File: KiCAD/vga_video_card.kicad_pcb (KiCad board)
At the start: 4 copper layers, 87 parts, among them J1 DE15_Socket_HighDensity, J2 Conn_01x20, J3 Conn_01x20, J4 Conn_01x20, J5 Conn_01x20, J6 Conn_02x20_Odd_Even, SW1 rst_btn, SW2 SW_DPDT_x2, SW3 SW_DPDT_x2, SW4 SW_DPDT_x2, U1 74HC161, U10 74HC04, U11 74HC112, U12 74HC32, U13 74HC173, U14 74HC173, U15 74HC161, U16 74HC161, U17 74HC161, U18 74HC04, U19 74HC04, U2 74HC161, U20 74HC133, U21 74HC133, U22 74HC133, U23 74HC133, U24 74HC112, U25 74HC173, U26 74HC173, U27 74HC04, U28 74HC253, U29 74HC253, U3 74HC161, U30 CY7C199, U31 CY7C199, U32 74AHC595, U33 74AHC595, U34 74AHC595, U35 AD7523JN, U36 LM358, U37 74HC257, U38 74HC257, U39 74HC02, U4 74HC04, U40 74HC74, U41 74HC00, U44 74HC257, U45 74HC257, U46 74HC257, U47 74HC257, U48 74HC257, U49 74HC257, U5 74HC04, U50 74HC257, U51 74HC257, U52 74HC4053, U53 74HC4053, U54 74HC4053, U55 74HC257, U56 74HC257, U6 74HC30, U7 74HC30, U8 74HC30, U9 74HC30, Y1 10MHz

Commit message: partially finished pcb layout
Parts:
- moved U28 278.1 mm to (74.9, 49.5), turned to 90 degrees
- moved U29 265.6 mm to (99.1, 49.5), turned to 90 degrees
- moved J5 255.2 mm to (77.5, 193.0), turned to 90 degrees
- moved U32 248.5 mm to (77.5, 165.1)
- moved J3 244.1 mm to (77.5, 186.7), turned to 90 degrees
- moved U40 243.7 mm to (132.1, 154.9)
- moved U33 240.9 mm to (97.8, 165.1)
- moved R4 237.4 mm to (88.9, 182.9), turned to 90 degrees
- moved R2 236.1 mm to (88.9, 172.7), turned to 90 degrees
- moved U34 233.5 mm to (118.1, 165.1)
- moved U41 231.9 mm to (132.1, 111.8)
- moved R5 230.9 mm to (94.0, 182.9), turned to 90 degrees
- moved RV1 230.4 mm to (127.0, 80.0)
- moved R3 229.6 mm to (94.0, 172.7), turned to 90 degrees
- moved J4 226.9 mm to (77.5, 154.9), turned to 90 degrees
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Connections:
- net /RAM_module/RAM_bus_mux/j_addr0 renamed /RAM_module/r_j_addr0
- J6 pad 10: /RAM_module/RAM_bus_mux/j_addr3 -> /RAM_module/r_j_addr3
- J6 pad 11: /RAM_module/RAM_bus_mux/i_addr4 -> /RAM_module/r_i_addr4
- J6 pad 12: /RAM_module/RAM_bus_mux/j_addr4 -> /RAM_module/r_j_addr4
- J6 pad 13: /RAM_module/RAM_bus_mux/i_addr5 -> /RAM_module/r_i_addr5
- J6 pad 14: /RAM_module/RAM_bus_mux/j_addr5 -> /RAM_module/r_j_addr5
- J6 pad 15: /RAM_module/RAM_bus_mux/i_addr6 -> /RAM_module/r_i_addr6
- J6 pad 16: /RAM_module/RAM_bus_mux/j_addr6 -> /RAM_module/r_j_addr6
- J6 pad 17: /RAM_module/RAM_bus_mux/i_addr7 -> /RAM_module/r_i_addr7
- J6 pad 18: /RAM_module/RAM_bus_mux/j_addr7 -> /RAM_module/r_j_addr7
- J6 pad 3: /RAM_module/RAM_bus_mux/i_addr0 -> /RAM_module/r_i_addr0
- J6 pad 5: /RAM_module/RAM_bus_mux/i_addr1 -> /RAM_module/r_i_addr1
- J6 pad 6: /RAM_module/RAM_bus_mux/j_addr1 -> /RAM_module/r_j_addr1
- J6 pad 7: /RAM_module/RAM_bus_mux/i_addr2 -> /RAM_module/r_i_addr2
- J6 pad 8: /RAM_module/RAM_bus_mux/j_addr2 -> /RAM_module/r_j_addr2
- J6 pad 9: /RAM_module/RAM_bus_mux/i_addr3 -> /RAM_module/r_i_addr3
- U13 pad 4: /RAM_module/RAM_bus_mux/j_addr1 -> /RAM_module/r_j_addr1
- U13 pad 5: /RAM_module/RAM_bus_mux/j_addr2 -> /RAM_module/r_j_addr2
- U13 pad 6: /RAM_module/RAM_bus_mux/j_addr3 -> /RAM_module/r_j_addr3
- U14 pad 3: /RAM_module/RAM_bus_mux/j_addr4 -> /RAM_module/r_j_addr4
- U14 pad 4: /RAM_module/RAM_bus_mux/j_addr5 -> /RAM_module/r_j_addr5
- U14 pad 5: /RAM_module/RAM_bus_mux/j_addr6 -> /RAM_module/r_j_addr6
- U14 pad 6: /RAM_module/RAM_bus_mux/j_addr7 -> /RAM_module/r_j_addr7
- U25 pad 3: /RAM_module/RAM_bus_mux/i_addr0 -> /RAM_module/r_i_addr0
- U25 pad 4: /RAM_module/RAM_bus_mux/i_addr1 -> /RAM_module/r_i_addr1
- U25 pad 5: /RAM_module/RAM_bus_mux/i_addr2 -> /RAM_module/r_i_addr2
- U25 pad 6: /RAM_module/RAM_bus_mux/i_addr3 -> /RAM_module/r_i_addr3
- U26 pad 3: /RAM_module/RAM_bus_mux/i_addr4 -> /RAM_module/r_i_addr4
- U26 pad 4: /RAM_module/RAM_bus_mux/i_addr5 -> /RAM_module/r_i_addr5
- U26 pad 5: /RAM_module/RAM_bus_mux/i_addr6 -> /RAM_module/r_i_addr6
- U26 pad 6: /RAM_module/RAM_bus_mux/i_addr7 -> /RAM_module/r_i_addr7
- U44 pad 11: /RAM_module/RAM_bus_mux/addr3 -> /RAM_module/r_i_addr3
- U44 pad 14: /RAM_module/RAM_bus_mux/addr2 -> /RAM_module/r_i_addr2
- U44 pad 2: /RAM_module/RAM_bus_mux/addr0 -> /RAM_module/r_i_addr0
- U44 pad 5: /RAM_module/RAM_bus_mux/addr1 -> /RAM_module/r_i_addr1
- U45 pad 11: /RAM_module/RAM_bus_mux/addr7 -> /RAM_module/r_i_addr7
- U45 pad 14: /RAM_module/RAM_bus_mux/addr6 -> /RAM_module/r_i_addr6
- U45 pad 2: /RAM_module/RAM_bus_mux/addr4 -> /RAM_module/r_i_addr4
- U45 pad 5: /RAM_module/RAM_bus_mux/addr5 -> /RAM_module/r_i_addr5
- U46 pad 11: /RAM_module/RAM_bus_mux/addr11 -> /RAM_module/r_j_addr4
- U46 pad 14: /RAM_module/RAM_bus_mux/addr10 -> /RAM_module/r_j_addr3
- U46 pad 2: /RAM_module/RAM_bus_mux/addr8 -> /RAM_module/r_j_addr1
- U46 pad 5: /RAM_module/RAM_bus_mux/addr9 -> /RAM_module/r_j_addr2
- U47 pad 14: /RAM_module/RAM_bus_mux/addr14 -> /RAM_module/r_j_addr7
- U47 pad 2: /RAM_module/RAM_bus_mux/addr12 -> /RAM_module/r_j_addr5
- U47 pad 5: /RAM_module/RAM_bus_mux/addr13 -> /RAM_module/r_j_addr6
- U48 pad 10: /RAM_module/RAM_bus_mux/addr3 -> /RAM_module/r_i_addr3
- U48 pad 13: /RAM_module/RAM_bus_mux/addr2 -> /RAM_module/r_i_addr2
- U48 pad 3: /RAM_module/RAM_bus_mux/addr0 -> /RAM_module/r_i_addr0
- U48 pad 6: /RAM_module/RAM_bus_mux/addr1 -> /RAM_module/r_i_addr1
- U49 pad 10: /RAM_module/RAM_bus_mux/addr7 -> /RAM_module/r_i_addr7
- U49 pad 13: /RAM_module/RAM_bus_mux/addr6 -> /RAM_module/r_i_addr6
- U49 pad 3: /RAM_module/RAM_bus_mux/addr4 -> /RAM_module/r_i_addr4
- U49 pad 6: /RAM_module/RAM_bus_mux/addr5 -> /RAM_module/r_i_addr5
- U50 pad 10: /RAM_module/RAM_bus_mux/addr11 -> /RAM_module/r_j_addr4
- U50 pad 13: /RAM_module/RAM_bus_mux/addr10 -> /RAM_module/r_j_addr3
- U50 pad 3: /RAM_module/RAM_bus_mux/addr8 -> /RAM_module/r_j_addr1
- U50 pad 6: /RAM_module/RAM_bus_mux/addr9 -> /RAM_module/r_j_addr2
- U51 pad 13: /RAM_module/RAM_bus_mux/addr14 -> /RAM_module/r_j_addr7
- U51 pad 3: /RAM_module/RAM_bus_mux/addr12 -> /RAM_module/r_j_addr5
- U51 pad 6: /RAM_module/RAM_bus_mux/addr13 -> /RAM_module/r_j_addr6
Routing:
- net +5V: track 0.00 -> 1217.3 mm, vias 0 -> 2
- net GND: track 0.00 -> 1176.5 mm
- net /RAM_module/r_j_addr0: track 0.00 -> 338.4 mm, vias 0 -> 4
- net /RAM_module/r_j_addr3: track 0.00 -> 281.1 mm, vias 0 -> 4
- net /RAM_module/r_j_addr7: track 0.00 -> 276.0 mm, vias 0 -> 2
- net /RAM_module/r_j_addr6: track 0.00 -> 269.5 mm, vias 0 -> 3
- net /h_sync: track 0.00 -> 266.6 mm, vias 0 -> 2
- net /RAM_module/r_j_addr5: track 0.00 -> 260.5 mm, vias 0 -> 5
- net /RAM_module/r_j_addr4: track 0.00 -> 250.6 mm, vias 0 -> 3
- net /RAM_module/r_j_addr2: track 0.00 -> 236.1 mm, vias 0 -> 2
- net /eo_line: track 0.00 -> 224.6 mm, vias 0 -> 3
- net /RAM_module/r_j_addr1: track 0.00 -> 224.5 mm, vias 0 -> 2
- net /RAM_module/RAM_bus_mux/w_addr1: track 0.00 -> 206.9 mm, vias 0 -> 3
- net /RAM_module/RAM_bus_mux/w_addr0: track 0.00 -> 205.3 mm, vias 0 -> 2
- net /RAM_module/RAM_bus_mux/w_addr14: track 0.00 -> 199.1 mm, vias 0 -> 2
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- added copper zone on In1.Cu, net GND
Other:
- board outline added: 132.1 x 186.7 mm

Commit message: finished layout
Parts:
- SW2, SW3, SW4: value SW_DPDT_x2 -> DPDT
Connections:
- SW2 pad 1: /ext_R -> /int_brightness
- SW2 pad 3: /int_brightness -> /ext_R
- SW3 pad 1: /ext_G -> /int_brightness
- SW3 pad 3: /int_brightness -> /ext_G
- SW4 pad 1: /ext_B -> /int_brightness
- SW4 pad 3: /int_brightness -> /ext_B
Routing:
- net /RAM_module/r_j_addr0: track 338.4 -> 403.6 mm, vias 4 -> 5
- net +5V: track 1217.3 -> 1242.3 mm
- net /vertical_counter/~{is_v_vis_area}: track 121.8 -> 141.8 mm
- net /horizontal_counter/~{is_h_vis_area}: track 160.6 -> 180.2 mm
- net /vertical_counter/bit_9: track 137.1 -> 139.7 mm, vias 1 -> 3
- net Net-(U24A-J): track 91.5 -> 94.0 mm
- net Net-(U11A-J): track 15.0 -> 17.6 mm
- net /horizontal_counter/eo_vis_200: track 69.1 -> 71.7 mm
- net /ext_G: track 125.3 -> 127.8 mm
- net /ext_B: track 135.8 -> 137.8 mm
- net /RAM_module/r_i_addr2: track 127.2 -> 125.6 mm
- net /ext_R: track 120.9 -> 122.0 mm, vias 1 -> 2
- net /int_brightness: track 146.5 -> 145.5 mm
- added copper zone on In2.Cu, net +5V
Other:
- board text added: "330"
- board text added: "VGA Video Card v0.1 author: Yitong Zhao"
- board text added: "esp32"

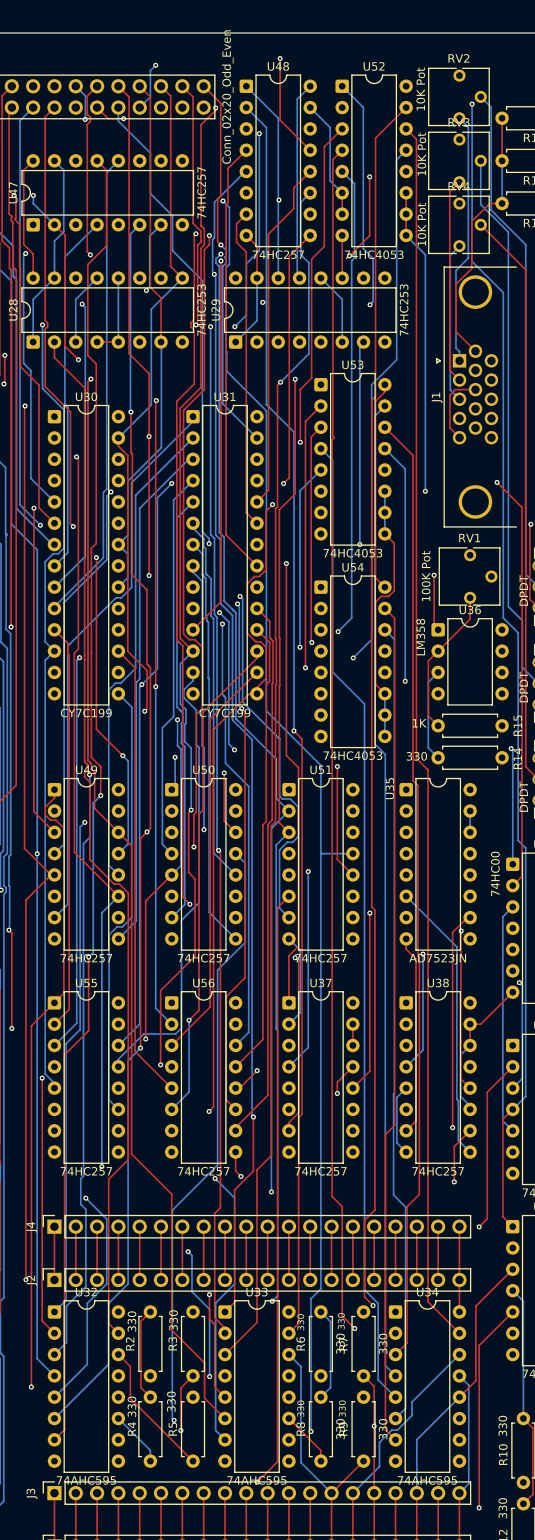
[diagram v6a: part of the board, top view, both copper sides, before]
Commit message: resolve DRC warnings
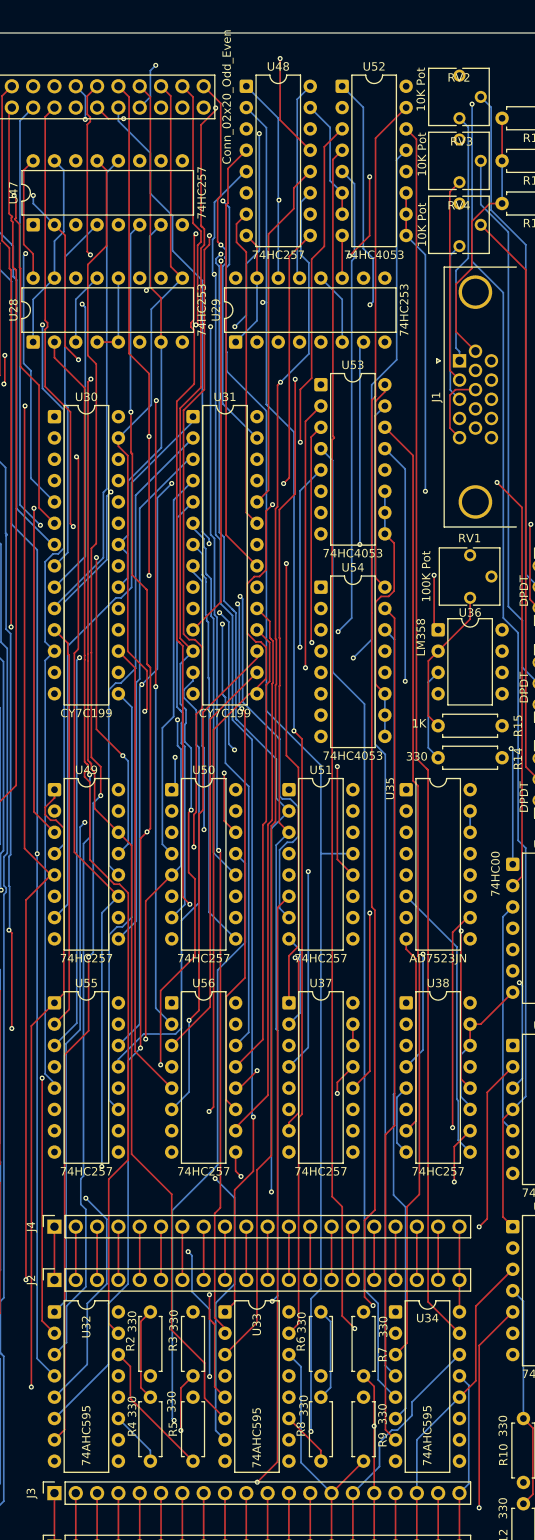
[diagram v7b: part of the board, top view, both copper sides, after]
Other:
- board text removed: "330"
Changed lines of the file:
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@@
 			(outputformat 1)
 			(mirror no)
-			(drillshape 1)
+			(drillshape 0)
 			(scaleselection 1)
 			(outputdirectory "")
@@
 		(tags "THT DIP DIL PDIP 2.54mm 7.62mm 300mil")
 		(property "Reference" "U34"
-			(at 3.81 -2.33 0)
+			(at 3.81 0.762 0)
 			(layer "F.SilkS")
 			(effects
@@
 		)
 		(property "Value" "74AHC595"
-			(at 3.81 20.11 0)
+			(at 3.81 14.732 90)
 			(layer "F.SilkS")
 			(effects
@@
 		(tags "Resistor Axial_DIN0207 series Axial Horizontal pin pitch 7.62mm 0.25W = 1/4W length 6.3mm diameter 2.5mm")
 		(property "Reference" "R7"
-			(at 3.81 -2.37 90)
+			(at 2.54 2.286 90)
 			(layer "F.SilkS")
 			(effects
@@
 		)
 		(property "Value" "330"
-			(at 3.81 2.37 90)
+			(at 5.842 2.37 90)
 			(layer "F.SilkS")
 			(effects
@@
 		(tags "THT DIP DIL PDIP 2.54mm 7.62mm 300mil")
 		(property "Reference" "U36"
-			(at 3.81 -2.33 0)
+			(at 3.81 -2.032 0)
 			(layer "F.SilkS")
 			(effects
@@
 		(tags "THT DIP DIL PDIP 2.54mm 7.62mm 300mil")
 		(property "Reference" "U33"
-			(at 3.81 -2.33 0)
+			(at 3.81 1.524 90)
 			(layer "F.SilkS")
 			(effects
@@
 		)
 		(property "Value" "74AHC595"
-			(at 3.81 20.11 0)
+			(at 3.81 14.986 90)
 			(layer "F.SilkS")
 			(effects
@@
 		(tags "Potentiometer vertical Vishay T73YP")
 		(property "Reference" "RV3"
-			(at -0.06 -7.09 0)
+			(at 0.254 -4.826 0)
 			(layer "F.SilkS")
 			(effects
@@
 		(tags "Potentiometer vertical Vishay T73YP")
 		(property "Reference" "RV2"
-			(at -0.06 -7.09 0)
+			(at -0.06 -4.826 0)
 			(layer "F.SilkS")
 			(effects
@@
 		)
 		(property "Value" "330"
-			(at 3.81 2.37 90)
+			(at 6.604 -2.032 90)
 			(layer "F.SilkS")
 			(effects
@@
 		(tags "Potentiometer vertical Vishay T73YP")
 		(property "Reference" "RV4"
-			(at -0.06 -7.09 0)
+			(at -0.06 -4.826 0)
 			(layer "F.SilkS")
 			(effects
@@
 		(tags "Resistor Axial_DIN0207 series Axial Horizontal pin pitch 7.62mm 0.25W = 1/4W length 6.3mm diameter 2.5mm")
 		(property "Reference" "R9"
-			(at 3.81 -2.37 90)
+			(at 2.54 2.286 90)
 			(layer "F.SilkS")
 			(effects
@@
 		)
 		(property "Value" "330"
-			(at 3.81 2.37 90)
+			(at 5.588 2.286 90)
 			(layer "F.SilkS")
 			(effects
@@
 		)
 		(property "Value" "330"
-			(at 3.81 2.37 90)
+			(at 6.35 -2.286 90)
 			(layer "F.SilkS")
 			(effects
@@
 		(tags "THT DIP DIL PDIP 2.54mm 7.62mm 300mil")
 		(property "Reference" "U32"
-			(at 3.81 -2.33 0)
+			(at 3.81 1.778 90)
 			(layer "F.SilkS")
 			(effects
@@
 		)
 		(property "Value" "74AHC595"
-			(at 3.81 20.11 0)
+			(at 3.81 14.732 90)
 			(layer "F.SilkS")
 			(effects
@@
 		(layer "Edge.Cuts")
 	)
-	(gr_text "330"
-		(at 107.315 167.386 90)
-		(layer "F.SilkS")
-		(effects
-			(font
-				(size 0.8 0.8)
-				(thickness 0.1)
-			)
-			(justify left bottom)
-		)
-	)
-	(gr_text "330"
-		(at 112.268 177.673 90)
-		(layer "F.SilkS")
-		(effects
-			(font
-				(size 0.8 0.8)
-				(thickness 0.1)
-			)
-			(justify left bottom)
-		)
-	)
-	(gr_text "330"
-		(at 107.315 177.673 90)
-		(layer "F.SilkS")
-		(effects
-			(font
-				(size 0.8 0.8)
-				(thickness 0.1)
-			)
-			(justify left bottom)
-		)
-	)
 	(gr_text "VGA Video Card v0.1\nauthor: Yitong Zhao"
 		(at 144.145 196.215 90)
@@
 				(thickness 0.1)
 			)
-			(justify left bottom)
-		)
-	)
-	(gr_text "330"
-		(at 112.141 167.259 90)
-		(layer "F.SilkS")
-		(effects
-			(font
-				(size 0.8 0.8)
-				(thickness 0.1)
-			)
